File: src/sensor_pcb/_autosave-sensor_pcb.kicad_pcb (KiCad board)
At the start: 2 copper layers, 34 parts, among them IC1 TCAN3414DRBR, J1 662004231722, J2 643280100305, J3 66200821022, J4 66200821022, J5 662004231722, J6 643280100305, Q2 NPN BJT 40V 200mA, Q3 NPN BJT 40V 200mA, U1 SHT45-AD1B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

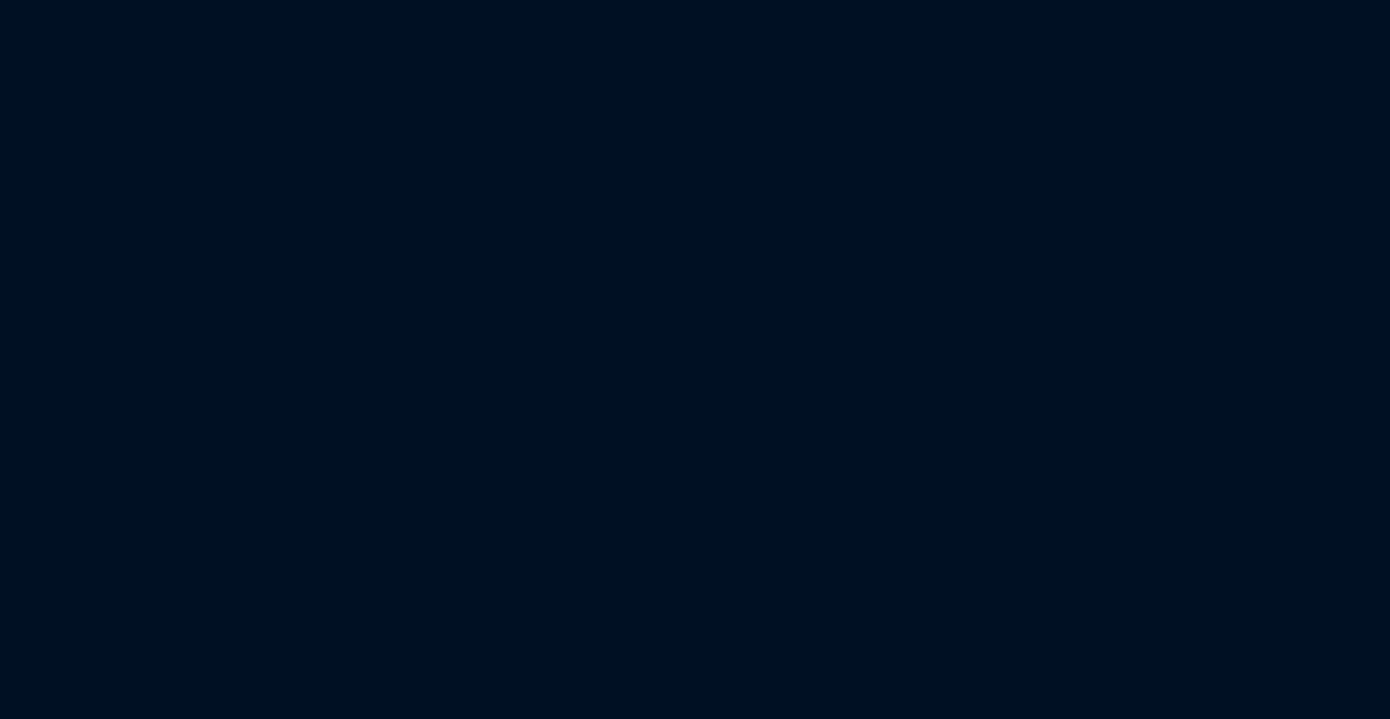
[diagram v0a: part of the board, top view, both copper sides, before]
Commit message: schematic update
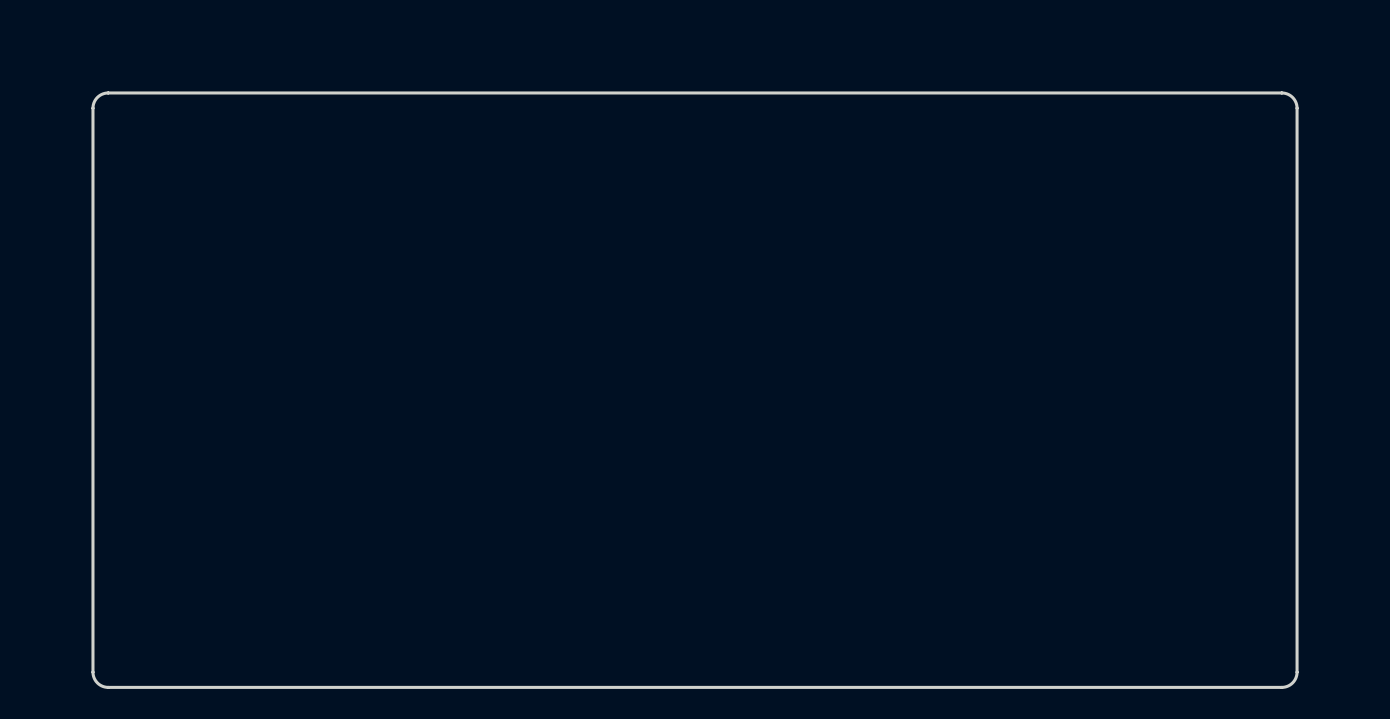
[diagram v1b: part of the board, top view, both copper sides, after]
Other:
- board outline added: 79 x 39 mm
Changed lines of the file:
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@@
 		)
+	)
+	(gr_line
+		(start 128 133)
+		(end 128 170)
+		(stroke
+			(width 0.2)
+			(type default)
+		)
+		(layer "Edge.Cuts")
+	)
+	(gr_arc
+		(start 128 170)
+		(mid 127.707107 170.707107)
+		(end 127 171)
+		(stroke
+			(width 0.2)
+			(type default)
+		)
+		(layer "Edge.Cuts")
+	)
+	(gr_arc
+		(start 49 133)
+		(mid 49.292893 132.292893)
+		(end 50 132)
+		(stroke
+			(width 0.2)
+			(type default)
+		)
+		(layer "Edge.Cuts")
+	)
+	(gr_line
+		(start 50 132)
+		(end 127 132)
+		(stroke
+			(width 0.2)
+			(type default)
+		)
+		(layer "Edge.Cuts")
+	)
+	(gr_arc
+		(start 50 171)
+		(mid 49.292893 170.707107)
+		(end 49 170)
+		(stroke
+			(width 0.2)
+			(type default)
+		)
+		(layer "Edge.Cuts")
+	)
+	(gr_arc
+		(start 127 132)
+		(mid 127.707107 132.292893)
+		(end 128 133)
+		(stroke
+			(width 0.2)
+			(type default)
+		)
+		(layer "Edge.Cuts")
+	)
+	(gr_line
+		(start 49 170)
+		(end 49 133)
+		(stroke
+			(width 0.2)
+			(type default)
+		)
+		(layer "Edge.Cuts")
+	)
+	(gr_line
+		(start 127 171)
+		(end 50 171)
+		(stroke
+			(width 0.2)
+			(type default)
+		)
+		(layer "Edge.Cuts")
 	)
 	(segment
